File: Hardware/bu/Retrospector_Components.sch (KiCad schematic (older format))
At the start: 145 parts, among them J1 SWD_Header, J2 Eurorack_10_pin_power, J3 Conn_01x08_Male, J4 Conn_01x08_Male, J5 Conn_01x08_Male, J6 Conn_01x08_Male, J7 USB_B_Micro, U1 STM32H743ZITx, U10 LM2675M-5, U11 TL072, U2 IS42S16800F-7TLI, U3 PCM5100APW, U4 SSI2164, U5 MCP6004, U6 MCP6004, U7 TL074, U8 LD1117-3.3-4Tab, Y1 8MHz 20pF

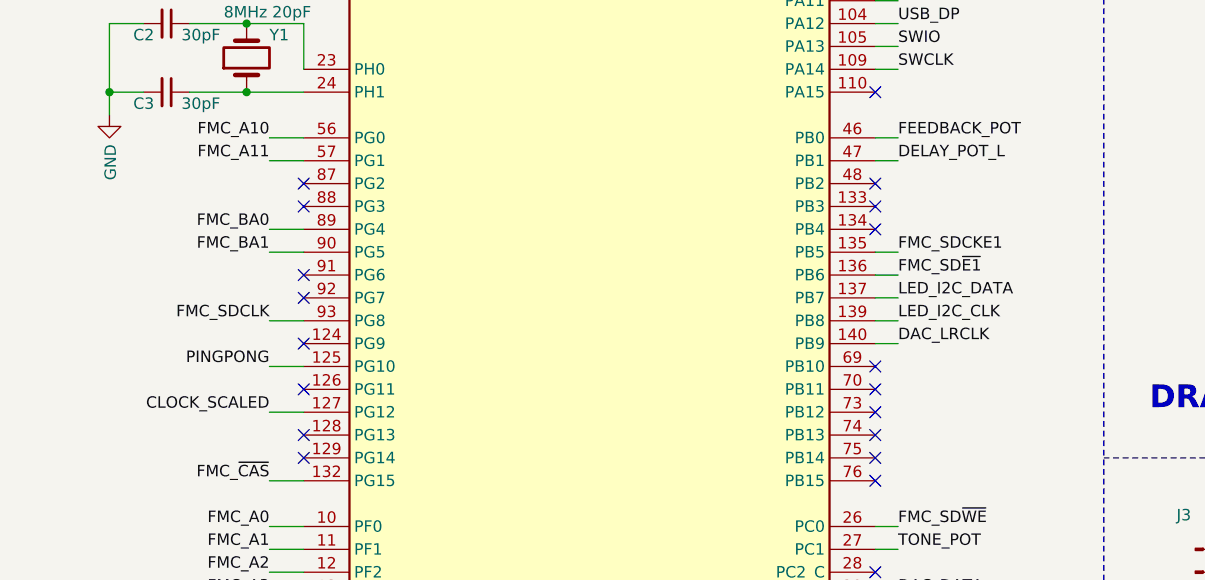
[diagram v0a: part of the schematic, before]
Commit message: Added some test code using SPI to control Toshiba LED controller
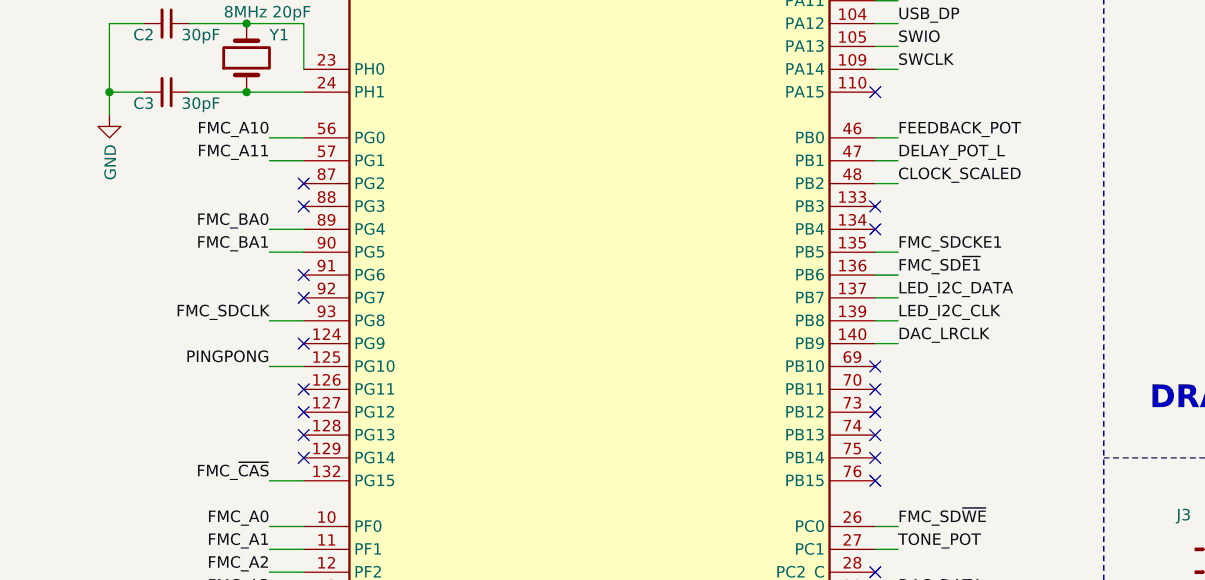
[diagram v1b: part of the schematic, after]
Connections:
- net CLOCK_SCALED: now also U1.48 (PB2); no longer U1.127 (PG12)
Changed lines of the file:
@@
 FMC_D15
 Wire Wire Line
-	2550 8850 2650 8850
-Connection ~ 2550 1650
-Wire Wire Line
-	2550 1650 2650 1650
-Connection ~ 2650 1650
-Wire Wire Line
-	2650 1650 2750 1650
-Connection ~ 2750 1650
-Wire Wire Line
-	2750 1650 2850 1650
-Connection ~ 2850 1650
-Wire Wire Line
 	3600 1300 3600 1400
 Wire Wire Line
@@
 	-1   0    0    1
 $EndComp
-Wire Wire Line
-	2850 1650 2950 1650
-Connection ~ 2950 1650
-Wire Wire Line
-	2950 1650 3050 1650
-Connection ~ 3050 1650
-Wire Wire Line
-	3050 1650 3150 1650
-Connection ~ 3150 1650
-Wire Wire Line
-	3150 1650 3250 1650
-Connection ~ 3250 1650
-Wire Wire Line
-	3250 1650 3350 1650
-Connection ~ 3350 1650
-Wire Wire Line
-	3350 1650 3450 1650
-Connection ~ 2650 8850
-Wire Wire Line
-	2650 8850 2750 8850
-Connection ~ 2750 8850
-Connection ~ 2850 8850
-Wire Wire Line
-	2850 8850 2950 8850
 Connection ~ 2950 8850
 Wire Wire Line
-	2750 8850 2850 8850
-Connection ~ 3050 8850
-Wire Wire Line
-	3050 8850 3150 8850
-Connection ~ 3150 8850
-Wire Wire Line
-	3150 8850 3250 8850
-Connection ~ 3250 8850
-Wire Wire Line
-	3250 8850 3350 8850
-Connection ~ 3450 1650
-Wire Wire Line
 	8100 2450 7750 2450
 Wire Wire Line
@@
 	5800 2250 6150 2250
 Wire Wire Line
-	3450 1650 3550 1650
-Wire Wire Line
 	4350 2450 4250 2450
 Wire Wire Line
@@
 NoConn ~ 4250 2950
 NoConn ~ 4250 3450
-NoConn ~ 4250 3850
 NoConn ~ 4250 3950
 NoConn ~ 4250 4050
@@
 	1050 10600 1200 10600
 Wire Wire Line
-	2950 8850 3050 8850
-Wire Wire Line
 	2950 8850 2950 9000
 $Comp
@@
 	1    0    0    -1
 $EndComp
-Wire Wire Line
-	3350 8850 3450 8850
-Connection ~ 3350 8850
 $Comp
 L Amplifier_Operational:MCP6004 U6
@@
 	4200 1000 3900 1000
 NoConn ~ 4250 4650
-Text Label 1600 4850 2    50   ~ 0
+Text Label 4350 3850 0    50   ~ 0
 CLOCK_SCALED
 Wire Wire Line
@@
 CHORUS
 Wire Wire Line
-	2450 1650 2550 1650
-Wire Wire Line
 	4250 6550 4350 6550
 NoConn ~ 4250 6050
 NoConn ~ 4250 6150
-Connection ~ 3550 1650
 Wire Wire Line
 	1750 3350 1750 3150
 $Comp
-L MCU_ST_STM32H7:STM32H743ZITx U1
-U 1 1 602FD32C
-P 3050 5250
-F 0 "U1" H 4050 1650 50  0000 C CNN
-F 1 "STM32H743ZITx" H 4100 1500 50  0000 C CNN
-F 2 "Package_QFP:LQFP-144_20x20mm_P0.5mm" H 1950 1850 50  0001 R CNN
-F 3 "http://www.st.com/st-web-ui/static/active/en/resource/technical/document/datasheet/DM00387108.pdf" H 3050 5250 50  0001 C CNN
-F 4 "C114408" H 3050 5250 50  0001 C CNN "Part_Number"
-F 5 "180" H 3050 5250 50  0001 C CNN "Rotation"
-	1    3050 5250
-	1    0    0    -1
-$EndComp
-Wire Wire Line
-	2350 1650 2450 1650
-Connection ~ 2450 1650
-$Comp
 L Connector:Conn_01x08_Male J6
 U 1 1 60832E97
@@
 	1600 4650 1750 4650
 Wire Wire Line
-	1600 4850 1750 4850
+	4350 3850 4250 3850
 $Comp
 L Connector:TestPoint TP10
@@
 	1    0    0    -1
 $EndComp
+Wire Wire Line
+	2950 8850 3050 8850
+Connection ~ 3050 8850
+Wire Wire Line
+	2850 8850 2950 8850
+Connection ~ 2850 8850
+Wire Wire Line
+	2750 8850 2850 8850
+Connection ~ 2750 8850
+Wire Wire Line
+	2650 8850 2750 8850
+Wire Wire Line
+	2550 8850 2650 8850
+Connection ~ 2650 8850
+Wire Wire Line
+	3350 8850 3450 8850
+Connection ~ 3350 8850
+Wire Wire Line
+	3250 8850 3350 8850
+Connection ~ 3250 8850
+Wire Wire Line
+	3150 8850 3250 8850
+Wire Wire Line
+	3050 8850 3150 8850
+Connection ~ 3150 8850
+Connection ~ 3550 1650
+Connection ~ 3050 1650
+Wire Wire Line
+	2950 1650 3050 1650
+Connection ~ 2950 1650
+Wire Wire Line
+	2850 1650 2950 1650
+Connection ~ 2850 1650
+Wire Wire Line
+	2750 1650 2850 1650
+Connection ~ 2750 1650
+Wire Wire Line
+	2650 1650 2750 1650
+Connection ~ 2650 1650
+Wire Wire Line
+	2550 1650 2650 1650
+Connection ~ 2550 1650
+Wire Wire Line
+	2350 1650 2450 1650
+Wire Wire Line
+	2450 1650 2550 1650
+Connection ~ 2450 1650
+Wire Wire Line
+	3450 1650 3550 1650
+Connection ~ 3450 1650
+Wire Wire Line
+	3350 1650 3450 1650
+Connection ~ 3350 1650
+Wire Wire Line
+	3250 1650 3350 1650
+Connection ~ 3250 1650
+Wire Wire Line
+	3150 1650 3250 1650
+Wire Wire Line
+	3050 1650 3150 1650
+Connection ~ 3150 1650
+$Comp
+L MCU_ST_STM32H7:STM32H743ZITx U1
+U 1 1 602FD32C
+P 3050 5250
+F 0 "U1" H 4050 1650 50  0000 C CNN
+F 1 "STM32H743ZITx" H 4100 1500 50  0000 C CNN
+F 2 "Package_QFP:LQFP-144_20x20mm_P0.5mm" H 1950 1850 50  0001 R CNN
+F 3 "http://www.st.com/st-web-ui/static/active/en/resource/technical/document/datasheet/DM00387108.pdf" H 3050 5250 50  0001 C CNN
+F 4 "C114408" H 3050 5250 50  0001 C CNN "Part_Number"
+F 5 "180" H 3050 5250 50  0001 C CNN "Rotation"
+	1    3050 5250
+	1    0    0    -1
+$EndComp
+NoConn ~ 1750 4850
 $EndSCHEMATC
